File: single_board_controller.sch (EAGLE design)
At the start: 82 parts, among them IC1 MCP3008, IC2 MCP3008, K1 AQ1AD2-3, K2 RELAY, P1 B9B-EH-A, Q1 NPN, Q2 NPN, Q3 NPN, Q4 NPN, Q5 NPN, Q6 NPN, Q7 TRANSISTIOR, Q8 TRANSISTIOR, T1 BTA41, U1 OPTOISOLATOR-2SOIC8, U2 OPTOISOLATOR-2SOIC8, U3 OPTOISOLATOR-2SOIC8, U4 OPTO-ISO

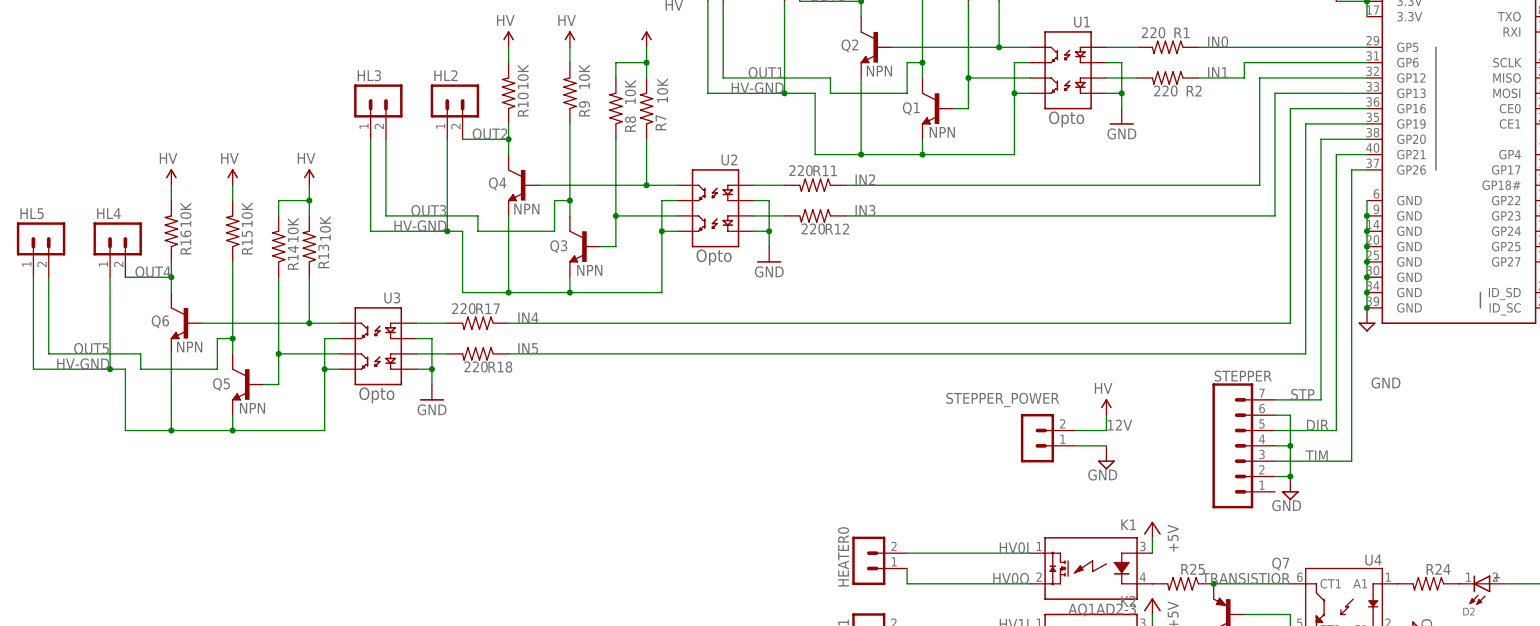
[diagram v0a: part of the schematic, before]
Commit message: placed the WOB header on brd, changed valve driver to two encoder headers, placed them on the brd
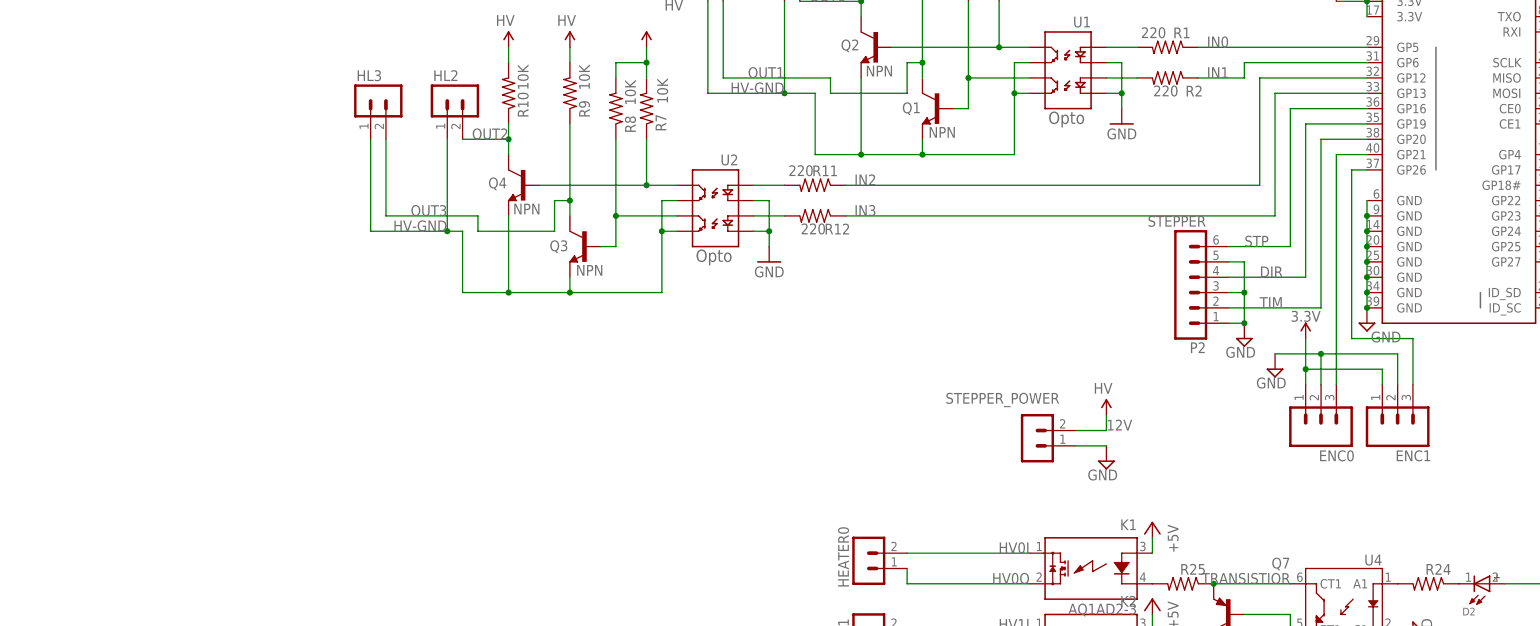
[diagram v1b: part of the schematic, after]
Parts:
- removed HL4, HL5: B2P-VH, con-jst-vh:B2P-VH
- removed Q5, Q6: NPN, SparkFun-DiscreteSemi:TRANSISTOR_NPNMMBT2222A
- removed R13, R14, R15, R16: 10K, SparkFun-Resistors:10KOHM1/10W1%(0603)0603
- removed R17, R18: 220, SparkFun-Resistors:220OHM-1/10W-1%(0603)
- removed STEPPER: (no value), SparkFun-Connectors:CONN_07
- removed U3: OPTOISOLATOR-2SOIC8, SparkFun-DiscreteSemi:OPTOISOLATOR-2SOIC8
- added ENC0, ENC1: (no value), SparkFun-Connectors:CONN_03JST-PTH-VERT
- added P2: STEPPER, con-jst-eh:B6B-EH-A
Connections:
- removed net IN4: R17.1, RASPBERRRY_PI_3_B+.GP16
- removed net IN5: R18.1, RASPBERRRY_PI_3_B+.GP19
- removed net OUT1N2: Q6.B, R13.1, U3.CL1
- removed net OUT2N2: Q5.B, R14.1, U3.CL2
- removed net OUT4: HL4.2, Q6.C, R16.1
- removed net OUT5: HL5.2, Q5.C, R15.1
- net 12V: no longer R13.2, R14.2, R15.2, R16.2
- net 3.3V: now also ENC0.1, ENC1.1
- net DIR: now also P2.4, RASPBERRRY_PI_3_B+.GP19; no longer RASPBERRRY_PI_3_B+.GP21, STEPPER.5
- net GND: now also ENC0.2, ENC1.2, P2.1, P2.3, P2.5; no longer STEPPER.2, STEPPER.4, STEPPER.6, U3.C1, U3.C2
- net HV-GND: no longer HL4.1, HL5.1, Q5.E, Q6.E, U3.EM1, U3.EM2
- net N$5: now also ENC1.3, RASPBERRRY_PI_3_B+.GP26; no longer R17.2, U3.A1
- net N$6: now also ENC0.3, RASPBERRRY_PI_3_B+.GP21; no longer R18.2, U3.A2
- net STP: now also P2.6, RASPBERRRY_PI_3_B+.GP16; no longer RASPBERRRY_PI_3_B+.GP20, STEPPER.7
- net TIM: now also P2.2, RASPBERRRY_PI_3_B+.GP20; no longer RASPBERRRY_PI_3_B+.GP26, STEPPER.3

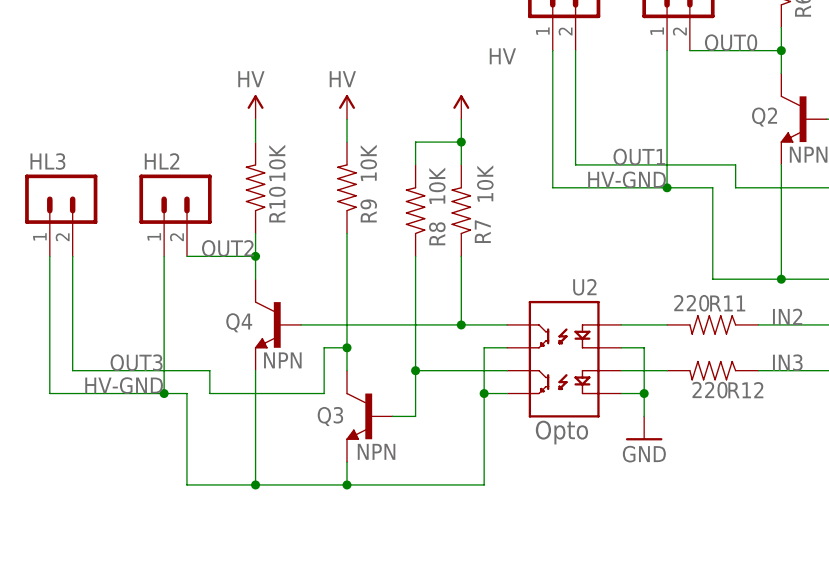
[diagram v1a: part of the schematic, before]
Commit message: began adding 12V driver
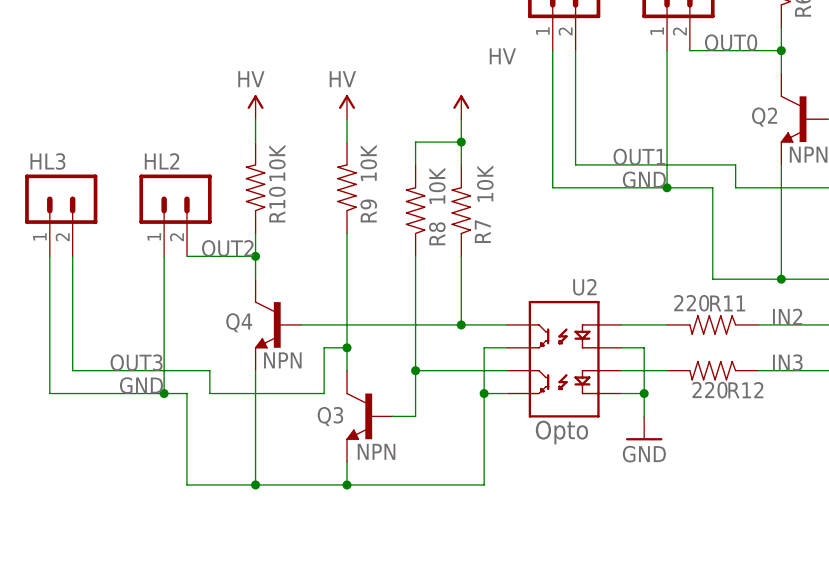
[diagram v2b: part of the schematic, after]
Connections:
- removed net HV-GND: HL0.1, HL1.1, HL2.1, HL3.1, Q1.E, Q2.E, Q3.E, Q4.E, U1.EM1, U1.EM2, U2.EM1, U2.EM2
- net GND: now also HL0.1, HL1.1, HL2.1, HL3.1, Q1.E, Q2.E, Q3.E, Q4.E, U1.EM1, U1.EM2, U2.EM1, U2.EM2
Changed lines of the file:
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@@
 <junction x="104.14" y="22.86"/>
 </segment>
-</net>
-<net name="5V" class="0">
-<segment>
-<pinref part="RASPBERRRY_PI_3_B+" gate="G$1" pin="5V@2"/>
-<pinref part="RASPBERRRY_PI_3_B+" gate="G$1" pin="5V@4"/>
-<wire x1="111.76" y1="86.36" x2="111.76" y2="83.82" width="0.1524" layer="91"/>
-<pinref part="SUPPLY4" gate="G$1" pin="5V"/>
-<junction x="111.76" y="86.36"/>
-</segment>
-<segment>
-<pinref part="WOB" gate="G$1" pin="1"/>
-<wire x1="165.1" y1="35.56" x2="157.48" y2="35.56" width="0.1524" layer="91"/>
-<label x="160.02" y="35.56" size="1.778" layer="95"/>
-<pinref part="SUPPLY11" gate="G$1" pin="5V"/>
-</segment>
-<segment>
-<wire x1="93.98" y1="99.06" x2="93.98" y2="96.52" width="0.1524" layer="91"/>
-<pinref part="SUPPLY19" gate="G$1" pin="5V"/>
-<junction x="93.98" y="99.06"/>
-<pinref part="5V_SUPPLY" gate="G$1" pin="2"/>
-</segment>
-</net>
-<net name="CUR1" class="0">
-<segment>
-<pinref part="IC1" gate="G$1" pin="CH5"/>
-<wire x1="236.22" y1="66.04" x2="256.54" y2="66.04" width="0.1524" layer="91"/>
-<label x="246.38" y="66.04" size="1.778" layer="95" rot="MR0"/>
-<pinref part="AMMETER1" gate="J$1" pin="3"/>
-<wire x1="256.54" y1="66.04" x2="256.54" y2="45.72" width="0.1524" layer="91"/>
-</segment>
-</net>
-<net name="N$1" class="0">
-<segment>
-<wire x1="73.66" y1="73.66" x2="68.58" y2="73.66" width="0.1524" layer="91"/>
-<pinref part="U1" gate="G$1" pin="A1"/>
-<pinref part="R1" gate="G$1" pin="2"/>
-</segment>
-</net>
-<net name="N$2" class="0">
-<segment>
-<wire x1="73.66" y1="68.58" x2="68.58" y2="68.58" width="0.1524" layer="91"/>
-<pinref part="U1" gate="G$1" pin="A2"/>
-<pinref part="R2" gate="G$1" pin="2"/>
-</segment>
-</net>
-<net name="HV-GND" class="0">
 <segment>
 <wire x1="55.88" y1="71.12" x2="53.34" y2="71.12" width="0.1524" layer="91"/>
@@
 </segment>
 </net>
+<net name="5V" class="0">
+<segment>
+<pinref part="RASPBERRRY_PI_3_B+" gate="G$1" pin="5V@2"/>
+<pinref part="RASPBERRRY_PI_3_B+" gate="G$1" pin="5V@4"/>
+<wire x1="111.76" y1="86.36" x2="111.76" y2="83.82" width="0.1524" layer="91"/>
+<pinref part="SUPPLY4" gate="G$1" pin="5V"/>
+<junction x="111.76" y="86.36"/>
+</segment>
+<segment>
+<pinref part="WOB" gate="G$1" pin="1"/>
+<wire x1="165.1" y1="35.56" x2="157.48" y2="35.56" width="0.1524" layer="91"/>
+<label x="160.02" y="35.56" size="1.778" layer="95"/>
+<pinref part="SUPPLY11" gate="G$1" pin="5V"/>
+</segment>
+<segment>
+<wire x1="93.98" y1="99.06" x2="93.98" y2="96.52" width="0.1524" layer="91"/>
+<pinref part="SUPPLY19" gate="G$1" pin="5V"/>
+<junction x="93.98" y="99.06"/>
+<pinref part="5V_SUPPLY" gate="G$1" pin="2"/>
+</segment>
+</net>
+<net name="CUR1" class="0">
+<segment>
+<pinref part="IC1" gate="G$1" pin="CH5"/>
+<wire x1="236.22" y1="66.04" x2="256.54" y2="66.04" width="0.1524" layer="91"/>
+<label x="246.38" y="66.04" size="1.778" layer="95" rot="MR0"/>
+<pinref part="AMMETER1" gate="J$1" pin="3"/>
+<wire x1="256.54" y1="66.04" x2="256.54" y2="45.72" width="0.1524" layer="91"/>
+</segment>
+</net>
+<net name="N$1" class="0">
+<segment>
+<wire x1="73.66" y1="73.66" x2="68.58" y2="73.66" width="0.1524" layer="91"/>
+<pinref part="U1" gate="G$1" pin="A1"/>
+<pinref part="R1" gate="G$1" pin="2"/>
+</segment>
+</net>
+<net name="N$2" class="0">
+<segment>
+<wire x1="73.66" y1="68.58" x2="68.58" y2="68.58" width="0.1524" layer="91"/>
+<pinref part="U1" gate="G$1" pin="A2"/>
+<pinref part="R2" gate="G$1" pin="2"/>
+</segment>
+</net>

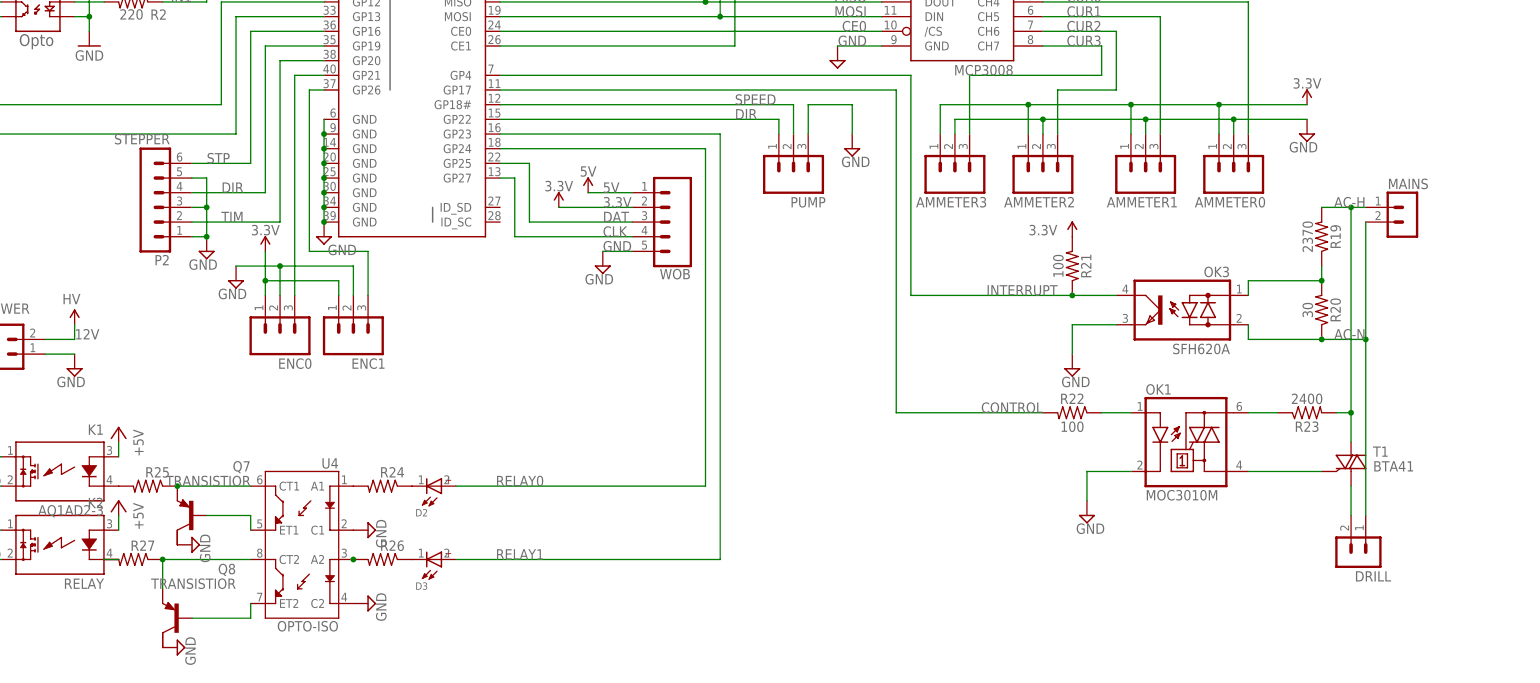
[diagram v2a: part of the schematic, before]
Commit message: began cleaning up stencils
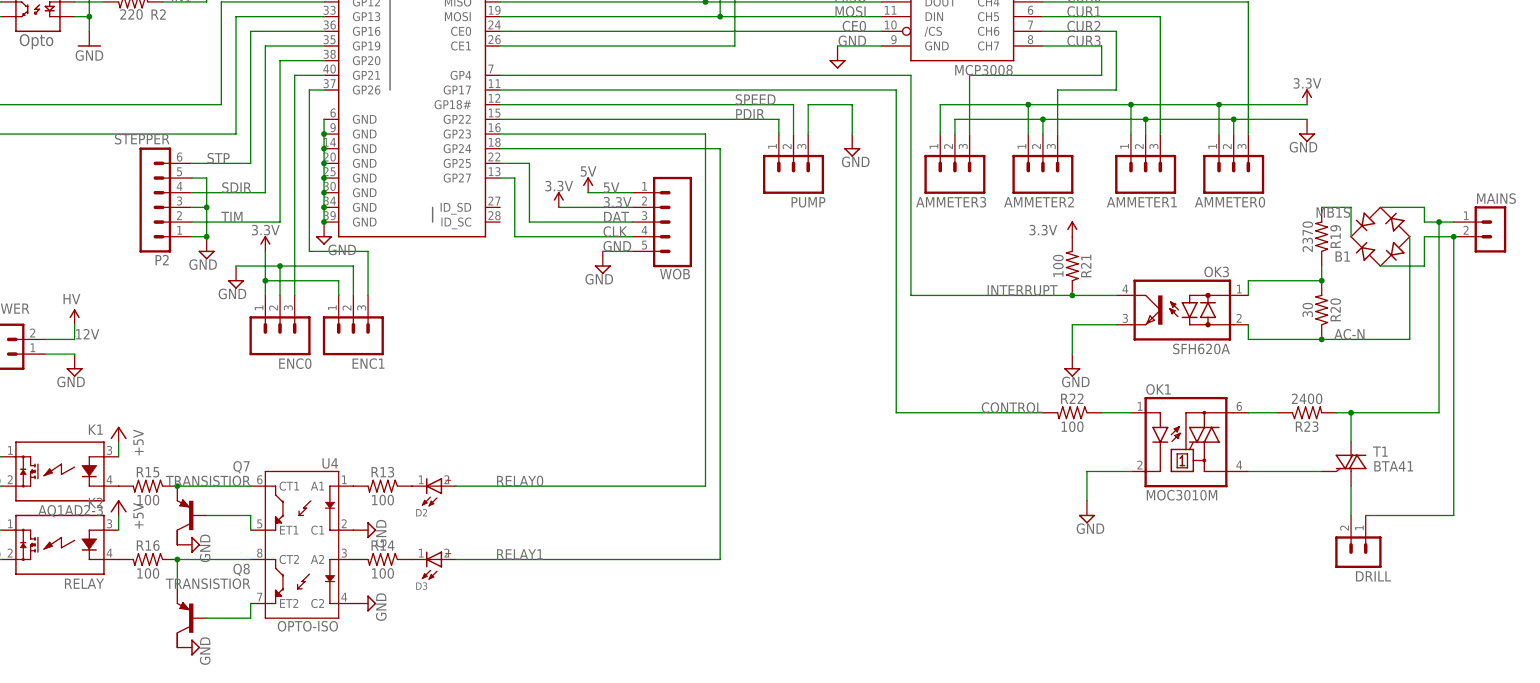
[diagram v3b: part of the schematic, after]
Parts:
- removed R24, R25, R26, R27: (no value), adafruit:FLIPFLOP-RES
- added B1: MB1S, rectifier:MB1S
- added R13, R14, R15, R16: 100, SparkFun-Resistors:0.3OHM-0805-1/8W-1%
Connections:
- removed net AC-H: MAINS.1, R19.2, R23.2, T1.A2
- removed net DIR: P2.4, PUMP.1, RASPBERRRY_PI_3_B+.GP19, RASPBERRRY_PI_3_B+.GP22
- new net N$24: B1.AC2, MAINS.1, R23.2, T1.A2
- new net N$25: B1.AC1, DRILL.1, MAINS.2
- new net N$26: B1.+, R19.2
- new net PDIR: PUMP.1, RASPBERRRY_PI_3_B+.GP22
- new net SDIR: P2.4, RASPBERRRY_PI_3_B+.GP19
- net AC-N: now also B1.-; no longer DRILL.1, MAINS.2
- net N$12: now also R13.2; no longer R24.2
- net N$13: now also R13.1; no longer R24.1
- net N$14: now also R14.2; no longer R26.2
- net N$15: now also R14.1; no longer R26.1
- net N$16: now also R15.1; no longer R25.1
- net N$17: now also R15.2; no longer R25.2
- net N$18: now also R16.1; no longer R27.1
- net N$19: now also R16.2; no longer R27.2
- net RELAY0: now also RASPBERRRY_PI_3_B+.GP23; no longer RASPBERRRY_PI_3_B+.GP24
- net RELAY1: now also RASPBERRRY_PI_3_B+.GP24; no longer RASPBERRRY_PI_3_B+.GP23
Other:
- moved on the sheet: MAINS, Q8
